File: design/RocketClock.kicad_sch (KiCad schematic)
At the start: 3 parts, among them P1 USB_C_Plug_USB2.0

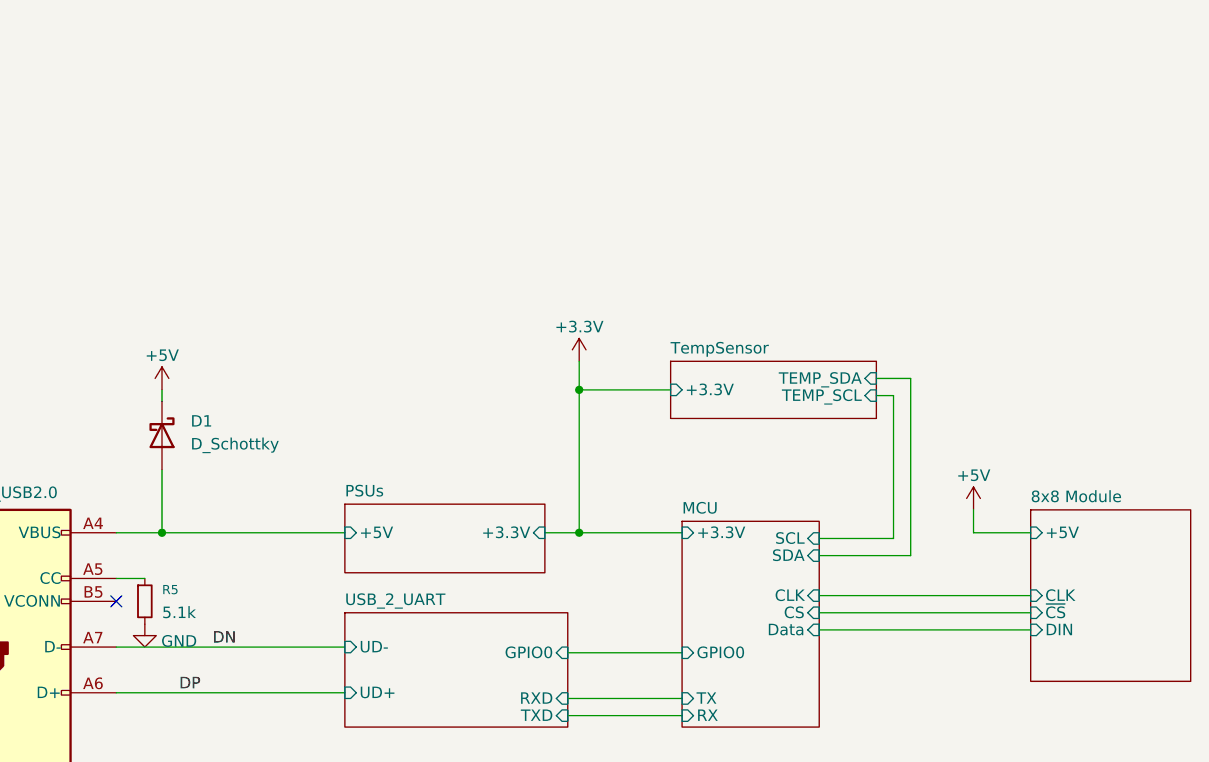
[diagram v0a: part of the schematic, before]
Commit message: Added some more sheets, new board layout
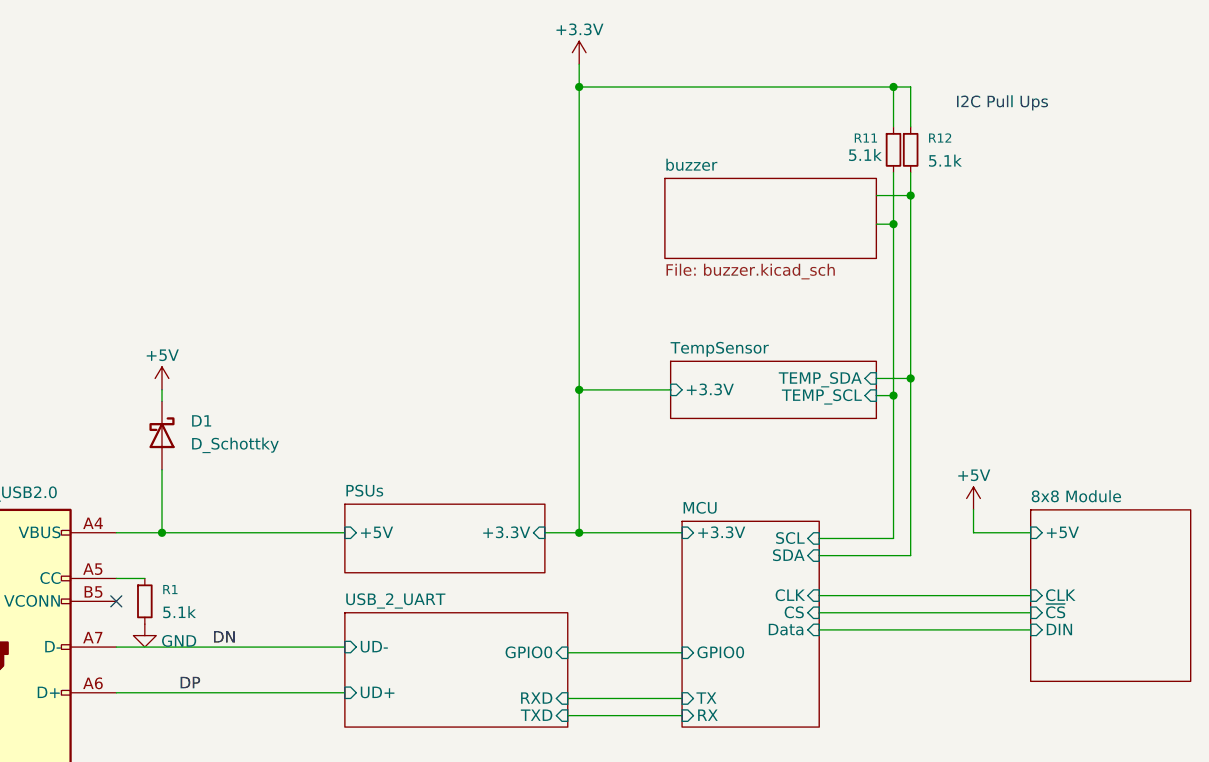
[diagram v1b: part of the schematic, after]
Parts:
- added R11, R12: 5.1k, Resistor_SMD:R_0402_1005Metric_Pad0.72x0.64mm_HandSolder, symbol Device:R_Small
- renumbered R5 to R1
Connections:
- net +3.3V: now also R11.1, R12.1
- net MCU/SCL: now also R11.2
- net MCU/SDA: now also R12.2
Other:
- added sheet buzzer (buzzer.kicad_sch)
- note added: "I2C Pull Ups"

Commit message: layout mostly done, schematic is done, need to generate new updated pdf
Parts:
- added J1: PROG_CONN, Connector_PinHeader_1.00mm:PinHeader_1x06_P1.00mm_Vertical_SMD_Pin1Left, symbol Connector_Generic:Conn_01x06
- added J2: Right Output Conn, Package_SO:MagConn, symbol Connector:Conn_01x05_Pin
- added J3: Left Input Conn, Package_SO:MagConn, symbol Connector:Conn_01x05_Pin
- P1: value USB_C_Plug_USB2.0 -> INPUT_PWR
- renumbered R11 to R1, R12 to R2, R1 to R3
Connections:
- net +3.3V: now also J1.1 (Pin_1)
- net +5V: now also J2.1 (Pin_1), J3.1 (Pin_1)
- net GND: now also J1.6 (Pin_6), J2.5 (Pin_5), J3.5 (Pin_5)
- net PSUs/+5V renamed VUSB
- new net CLK: J2.2 (Pin_2), J3.2 (Pin_2)
- new net DIN: J3.3 (Pin_3)
- new net DOUT: J2.3 (Pin_3)
- new net MISO: J1.3 (Pin_3)
- new net MOSI: J1.4 (Pin_4)
- new net RESET: J1.2 (Pin_2)
- new net SCK: J1.5 (Pin_5)
- new net ~{CS}: J2.4 (Pin_4), J3.4 (Pin_4)
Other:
- sheet 8x8 Module ports: added DOUT; removed none
- sheet MCU ports: added ~{CS}, ~{RST}; removed CS
- sheet USB_2_UART ports: added ~{RST}; removed none
- sheet buzzer ports: added +3V3, BUZZER_SCL, BUZZER_SDA, MISO, MOSI, RESET, SCK, ~{trigger}; removed none
- note added: "Could be a good idea to fuse this"
- note added: "Programming Connector"
- moved on the sheet: D1, P1, R1, R2, R3

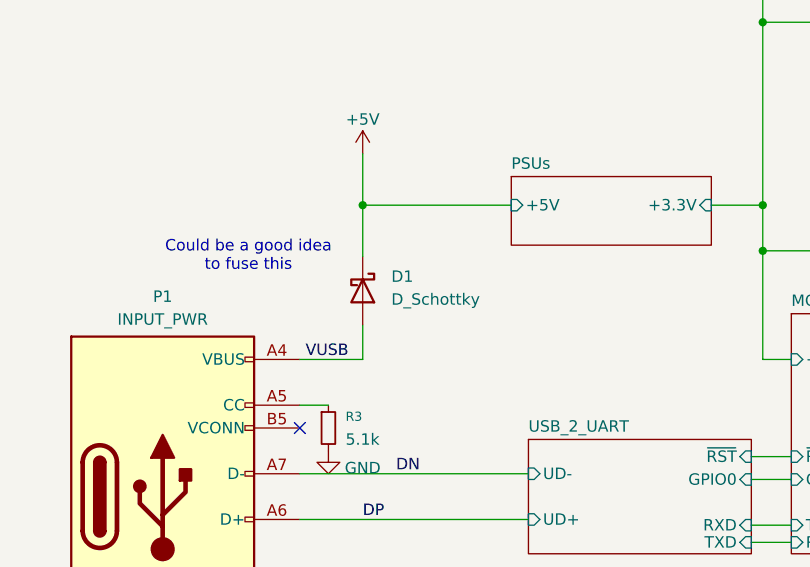
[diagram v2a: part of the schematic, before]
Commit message: Layout and Schematic Done
Almost ready for first release with tag. DRC etc passing, DFM checks pass on JLCPCB, but I need to go through sourcing components and ensure we have them all available before pushing the button on the orders
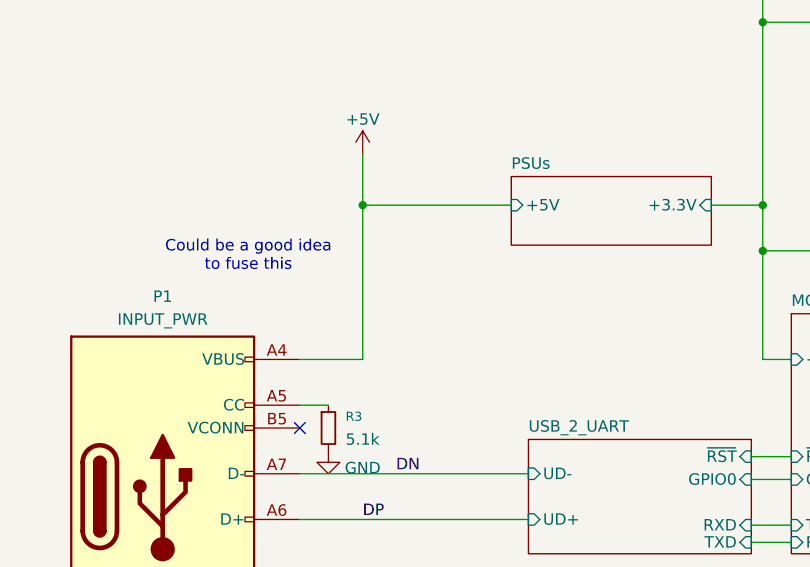
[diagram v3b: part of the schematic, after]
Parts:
- removed D1: D_Schottky, Diode_SMD:D_SOD-123, symbol Device:D_Schottky
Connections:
- net VUSB is gone; now on net +5V: P1.A4 (VBUS), P1.A9 (VBUS), P1.B4 (VBUS), P1.B9 (VBUS)
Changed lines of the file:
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@@
+	(wire
+		(pts
+			(xy 90.805 91.44) (xy 90.805 108.585)
+		)
+		(stroke
+			(width 0)
+			(type default)
+		)
+	)
 	(wire
 		(pts
@@
 	(wire
 		(pts
-			(xy 90.805 104.775) (xy 90.805 108.585)
-		)
-		(stroke
-			(width 0)
-			(type default)
-		)
-	)
-	(wire
-		(pts
 			(xy 83.82 126.365) (xy 109.22 126.365)
 		)
@@
 		(pts
 			(xy 135.255 108.585) (xy 138.43 108.585)
-		)
-		(stroke
-			(width 0)
-			(type default)
-		)
-	)
-	(wire
-		(pts
-			(xy 90.805 91.44) (xy 90.805 97.155)
 		)
 		(stroke
@@
 			)
 			(justify right bottom)
-		)
-	)
-	(label "VUSB"
-		(at 84.455 108.585 0)
-		(effects
-			(font
-				(size 1.27 1.27)
-			)
-			(justify left bottom)
 		)
 	)
@@
 					(unit 1)
 				)
-			)
-		)
-	)
-	(symbol
-		(lib_id "Device:D_Schottky")
-		(at 90.805 100.965 270)
-		(unit 1)
-		(exclude_from_sim no)
-		(in_bom yes)
-		(on_board yes)
-		(dnp no)
-		(fields_autoplaced yes)
-		(property "Reference" "D1"
-			(at 93.98 99.3774 90)
-			(effects
-				(font
-					(size 1.27 1.27)
-				)
-				(justify left)
-			)
-		)
-		(property "Value" "D_Schottky"
-			(at 93.98 101.9174 90)
-			(effects
-				(font
-					(size 1.27 1.27)
-				)
-				(justify left)
-			)
-		)
-		(property "Footprint" "Diode_SMD:D_SOD-123"
-			(at 90.805 100.965 0)
-			(effects
-				(font
-					(size 1.27 1.27)
-				)
-				(hide yes)
-			)
-		)
-		(property "Datasheet" "~"
-			(at 90.805 100.965 0)
-			(effects
-				(font
-					(size 1.27 1.27)
-				)
-				(hide yes)
-			)
-		)
-		(property "Description" "Schottky diode"
-			(at 90.805 100.965 0)
-			(effects
-				(font
-					(size 1.27 1.27)
-				)
-				(hide yes)
-			)
-		)
-		(pin "2"
-		)
-		(pin "1"
-		)
-		(instances
-			(project ""
-				(path "/e36fbef8-3f03-40ce-b8c1-50d21e162c91"
-					(reference "D1")
-					(unit 1)
-				)
